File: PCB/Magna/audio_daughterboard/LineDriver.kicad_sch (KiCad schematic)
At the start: 28 parts, among them J701 PSG01550, U701 NE5532, U702 NE5532, U703 NE5532

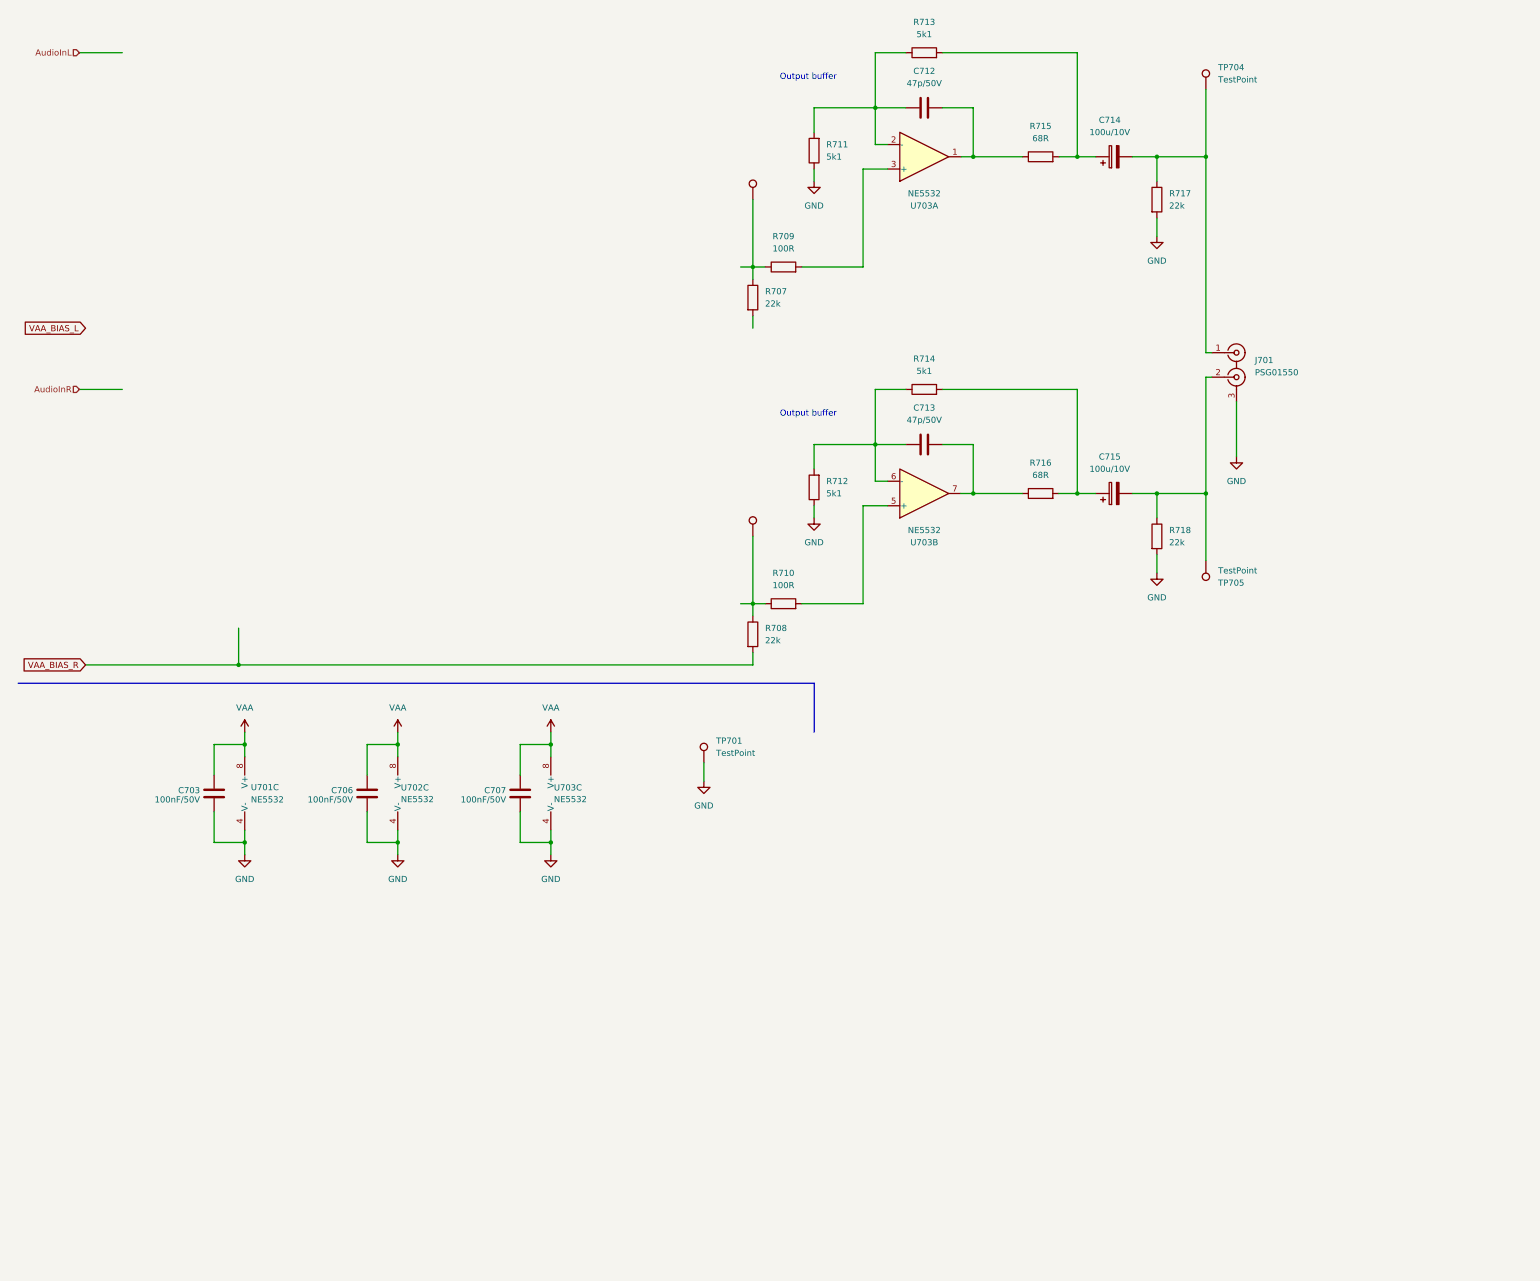
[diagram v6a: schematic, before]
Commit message: Update audio PCB
Mainly added simulations to Linedriver and DAC.

Also fixed some small issues that was found when simulating
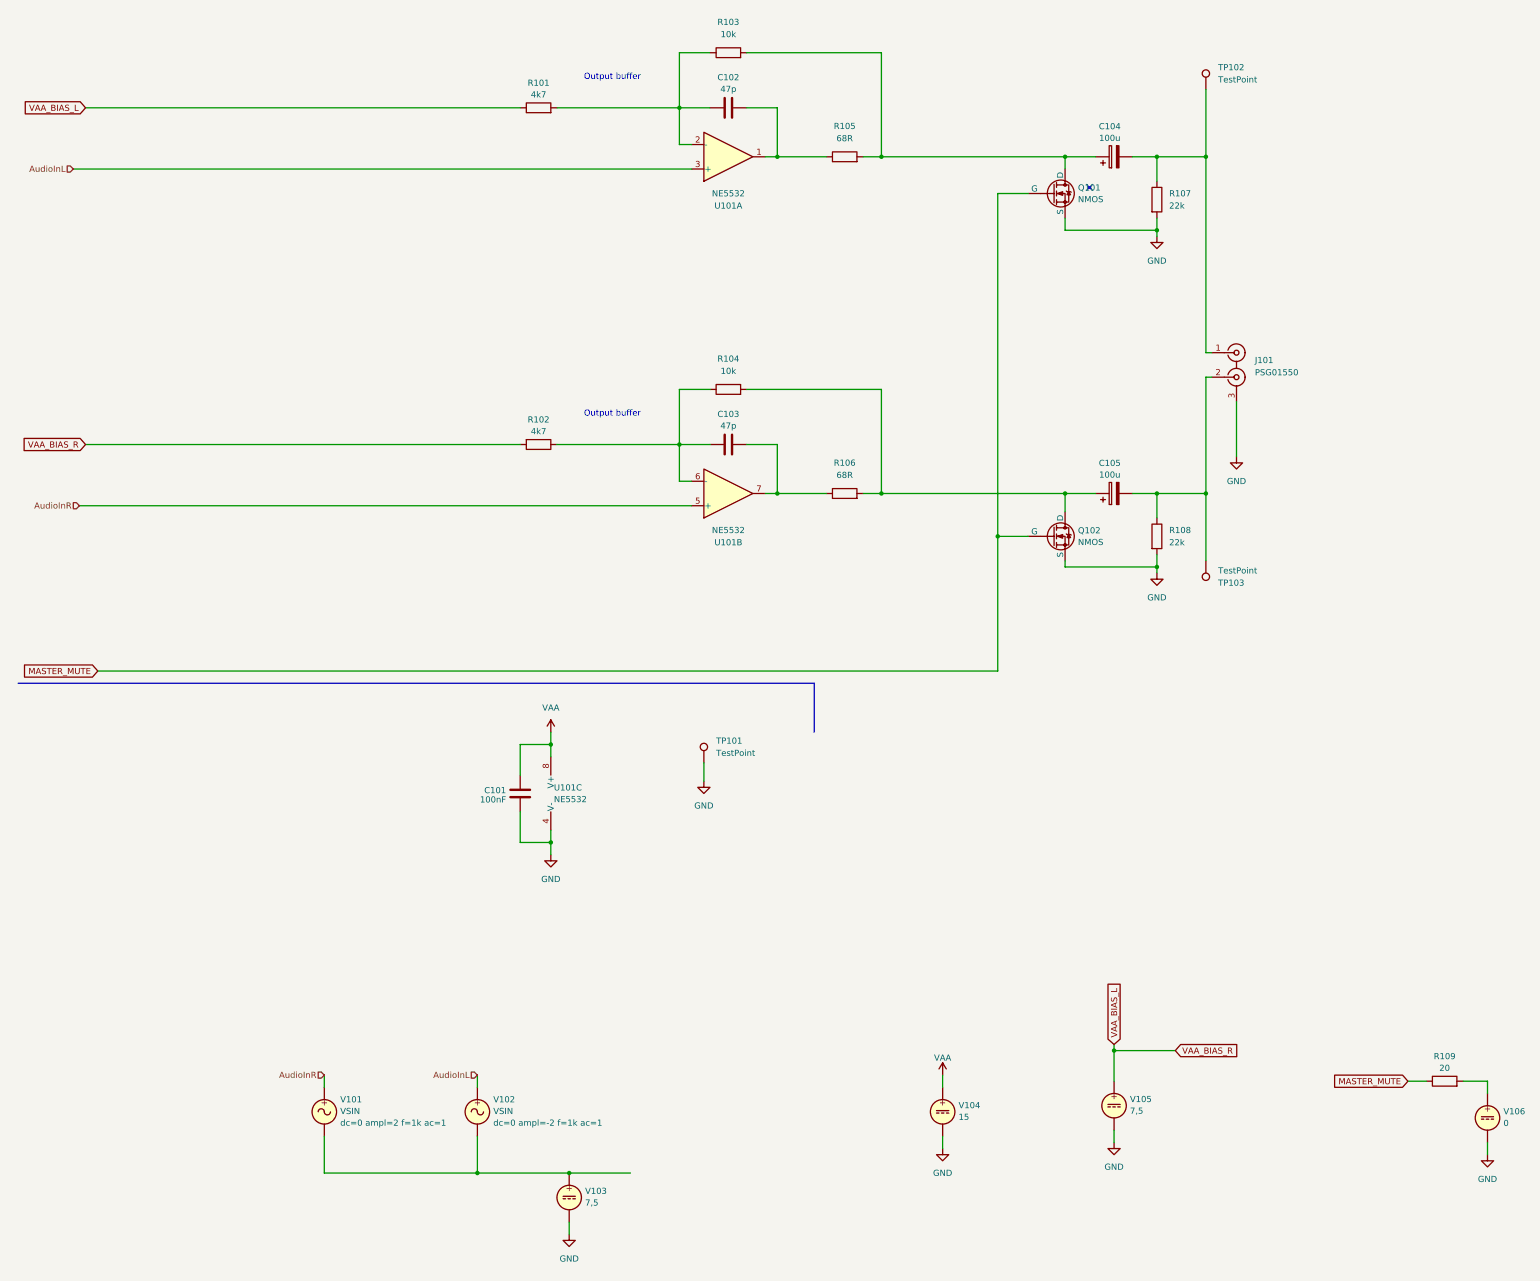
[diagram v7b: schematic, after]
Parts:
- removed C703, C706: 100nF/50V, Capacitor_SMD:C_0805_2012Metric_Pad1.18x1.45mm_HandSolder, symbol Device:C
- removed R707, R708: 22k, Resistor_SMD:R_0805_2012Metric_Pad1.20x1.40mm_HandSolder, symbol Device:R
- removed R709, R710: 100R, Resistor_SMD:R_0805_2012Metric_Pad1.20x1.40mm_HandSolder, symbol Device:R
- removed TP702, TP703: TestPoint, TestPoint:TestPoint_Keystone_5005-5009_Compact, symbol Connector:TestPoint
- removed U701, U702: NE5532, Package_SO:SOIC-8_3.9x4.9mm_P1.27mm, symbol Amplifier_Operational:NE5532
- added Q101, Q102: NMOS, symbol Simulation_SPICE:NMOS
- added R109: 20, Resistor_SMD:R_0805_2012Metric_Pad1.20x1.40mm_HandSolder, symbol Device:R
- added V101, V102: VSIN, symbol Simulation_SPICE:VSIN
- added V103, V105: 7,5, symbol Simulation_SPICE:VDC
- added V104: 15, symbol Simulation_SPICE:VDC
- added V106: 0, symbol Simulation_SPICE:VDC
- C101: renamed from C707; value 100nF/50V -> 100nF
- C102: renamed from C712; value 47p/50V -> 47p
- C103: renamed from C713; value 47p/50V -> 47p
- C104: renamed from C714; value 100u/10V -> 100u
- C105: renamed from C715; value 100u/10V -> 100u
- R101: renamed from R711; value 5k1 -> 4k7; LCSC C218638 -> (none)
- R102: renamed from R712; value 5k1 -> 4k7; LCSC C218638 -> (none)
- R103: renamed from R713; value 5k1 -> 10k; LCSC C218638 -> (none)
- R104: renamed from R714; value 5k1 -> 10k; LCSC C218638 -> (none)
- renumbered J701 to J101, R715 to R105, R716 to R106, R717 to R107, R718 to R108, TP701 to TP101, TP704 to TP102, TP705 to TP103, U703 to U101
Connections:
- net AudioInL: now also U101.3 (+), V102.1
- net AudioInR: now also U101.5 (+), V101.1
- net GND: now also Q101.3 (S), Q102.3 (S), V103.2, V104.2, V105.2, V106.2; no longer R101.1, R102.1
- net VAA: now also V104.1
- net VAA_BIAS_L: now also R101.1, R102.2, V105.1
- net at C105.1, R104.2, R106.2: now also Q102.1 (D)
- net at C103.1, R104.1, U101.6 (-): now also R102.1; no longer R102.2
- net at C104.1, R103.2, R105.2: now also Q101.1 (D)
- new net: R109.2, V106.1
- new net: V101.2, V102.2, V103.1
- new net MASTER_MUTE: Q101.2 (G), Q102.2 (G), R109.1
- no-connect marks 0 -> 1
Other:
- moved on the sheet: C102, C103, R101, R102, R103, R104, R105, R106, U101A, U101B

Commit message: "Finalize" Audio daugherboard
Finished DAC output filter
Fixed the whole damn MCU subschematic
Fixed Linedriver schematic
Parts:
- removed C105: 100u, Capacitor_SMD:CP_Elec_6.3x5.8, symbol Device:C_Polarized
- added C705: 100u, Capacitor_SMD:CP_Elec_6.3x5.8, symbol Device:C_Polarized
- added R701, R702: 1k1, symbol Device:R
- added R703, R704: 100, symbol Device:R
- added V706: 7,5, symbol Simulation_SPICE:VDC
- renumbered C101 to C701, C102 to C702, C103 to C703, C104 to C704, J101 to J701, Q101 to Q701, Q102 to Q702, R101 to R705, R102 to R706, R103 to R707, R104 to R708, R105 to R709, R106 to R710, R109 to R711, R107 to R712, R108 to R713, TP101 to TP701, TP102 to TP702, TP103 to TP703, U101 to U701, V101 to V701, V102 to V702, V103 to V703, V104 to V704, V105 to V705, V106 to V707
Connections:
- net AudioInL: now also R701.1; no longer U701.3 (+)
- net AudioInR: now also R702.1; no longer U701.5 (+)
- net GND: now also V706.2
- net VAA_BIAS_L: now also R703.1; no longer R706.2
- net at J701.2 (IN2), R713.1, TP703.1: now also C705.2
- net at Q702.1 (D), R708.2, R710.2: now also C705.1
- new net: R702.2, R704.2, U701.5 (+)
- new net: R701.2, R703.2, U701.3 (+)
- new net VAA_BIAS_R: R704.1, R706.2, V706.1
- no-connect marks 1 -> 0
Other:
- note added: "Audio in has a P2P voltage of 9V, Line output should be 3.5V P2P. So voltage is divided to make sure the output is not too hot."
- moved on the sheet: R711, V704, V705, V707
